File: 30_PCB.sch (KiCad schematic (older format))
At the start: 35 parts, among them J1 IPM-165-Radar, J10 TEST_VCC, J11 TEST_OUT, J2 TEST_AMPLIN, J3 TEST_AMPL1_OUT, J4 TEST_AMPL2_OUT, J6 TEST_GNDD, J7 TEST_GNDD, J8 TEST_GNDA, J9 TEST_GNDA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

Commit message: PCB R0.5/Schema R0.6
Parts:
- added R12: 1k, Resistor_SMD:R_1206_3216Metric_Pad1.42x1.75mm_HandSolder, symbol Device:R
- added unit 3 of U1
- C1, C2, C5: footprint Capacitor_THT:C_Radial_D5.0mm_H11.0mm_P2.00mm -> Capacitor_THT:CP_Radial_D5.0mm_P2.00mm
- C4: footprint Capacitor_THT:C_Rect_L7.2mm_W3.5mm_P5.00mm_FKS2_FKP2_MKS2_MKP2 -> Capacitor_THT:C_Rect_L7.2mm_W2.5mm_P5.00mm_FKS2_FKP2_MKS2_MKP2
- C6: footprint Capacitor_THT:C_Rect_L7.2mm_W5.5mm_P5.00mm_FKS2_FKP2_MKS2_MKP2 -> Capacitor_THT:C_Rect_L7.2mm_W4.5mm_P5.00mm_FKS2_FKP2_MKS2_MKP2
- D1, D2, D3, D4: footprint Diode_SMD:D_1206_3216Metric -> Diode_SMD:D_1206_3216Metric_Pad1.42x1.75mm_HandSolder
- R10, R11, R7, R9: footprint Resistor_SMD:R_1206_3216Metric -> Resistor_SMD:R_1206_3216Metric_Pad1.42x1.75mm_HandSolder
- XA1: symbol Arduino_SDHD:Arduino_Uno_Shield -> 30_PCB-rescue:Arduino_Uno_Shield-Arduino_SDHD
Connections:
- net GNDA: now also U1.4 (V-)
- net GNDD: now also R12.1
- net VCC: now also U1.8 (V+)
- net at SW1.2, SW1.4, XA1.D4: now also R12.2
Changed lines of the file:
@@
 Title "24GHz Radar Movement Detector"
 Date "2020-05-5"
-Rev "R0.5"
+Rev "R0.6"
 Comp "Hochschule Darmstadt"
 Comment1 ""
@@
 F 0 "C5" V 3625 4300 50  0000 C CNN
 F 1 "4.7u" V 3716 4300 50  0000 C CNN
-F 2 "Capacitor_THT:C_Radial_D5.0mm_H11.0mm_P2.00mm" H 3850 4300 50  0001 C CNN
+F 2 "Capacitor_THT:CP_Radial_D5.0mm_P2.00mm" H 3850 4300 50  0001 C CNN
 F 3 "~" H 3850 4300 50  0001 C CNN
 	1    3850 4300
@@
 F 0 "C2" V 1925 4400 50  0000 C CNN
 F 1 "4.7u" V 1834 4400 50  0000 C CNN
-F 2 "Capacitor_THT:C_Radial_D5.0mm_H11.0mm_P2.00mm" H 1700 4400 50  0001 C CNN
+F 2 "Capacitor_THT:CP_Radial_D5.0mm_P2.00mm" H 1700 4400 50  0001 C CNN
 F 3 "~" H 1700 4400 50  0001 C CNN
 	1    1700 4400
@@
 F 0 "C6" V 4698 5450 50  0000 C CNN
 F 1 "3.3n" V 4789 5450 50  0000 C CNN
-F 2 "Capacitor_THT:C_Rect_L7.2mm_W5.5mm_P5.00mm_FKS2_FKP2_MKS2_MKP2" H 4988 5300 50  0001 C CNN
+F 2 "Capacitor_THT:C_Rect_L7.2mm_W4.5mm_P5.00mm_FKS2_FKP2_MKS2_MKP2" H 4988 5300 50  0001 C CNN
 F 3 "~" H 4950 5450 50  0001 C CNN
 	1    4950 5450
@@
 F 0 "C1" H 1288 3146 50  0000 L CNN
 F 1 "22u" H 1288 3055 50  0000 L CNN
-F 2 "Capacitor_THT:C_Radial_D5.0mm_H11.0mm_P2.00mm" H 1200 3100 50  0001 C CNN
+F 2 "Capacitor_THT:CP_Radial_D5.0mm_P2.00mm" H 1200 3100 50  0001 C CNN
 F 3 "~" H 1200 3100 50  0001 C CNN
 	1    1200 3100
@@
 F 0 "C4" H 3238 3196 50  0000 L CNN
 F 1 "100n" H 3238 3105 50  0000 L CNN
-F 2 "Capacitor_THT:C_Rect_L7.2mm_W3.5mm_P5.00mm_FKS2_FKP2_MKS2_MKP2" H 3150 3150 50  0001 C CNN
+F 2 "Capacitor_THT:C_Rect_L7.2mm_W2.5mm_P5.00mm_FKS2_FKP2_MKS2_MKP2" H 3150 3150 50  0001 C CNN
 F 3 "~" H 3150 3150 50  0001 C CNN
 	1    3150 3150
@@
 $EndComp
 $Comp
-L Arduino_SDHD:Arduino_Uno_Shield XA1
+L 30_PCB-rescue:Arduino_Uno_Shield-Arduino_SDHD XA1
 U 1 1 5EBD5CC3
 P 7800 4050
@@
 F 0 "D2" H 9700 4150 50  0000 R CNN
 F 1 "GREEN" H 9500 4350 50  0000 R CNN
-F 2 "Diode_SMD:D_1206_3216Metric" H 9600 4250 50  0001 C CNN
+F 2 "Diode_SMD:D_1206_3216Metric_Pad1.42x1.75mm_HandSolder" H 9600 4250 50  0001 C CNN
 F 3 "~" H 9600 4250 50  0001 C CNN
 	1    9600 4250
@@
 F 0 "R11" H 10250 3900 50  0000 L CNN
 F 1 "220" V 10100 3650 50  0000 L CNN
-F 2 "Resistor_SMD:R_1206_3216Metric" V 10130 3750 50  0001 C CNN
+F 2 "Resistor_SMD:R_1206_3216Metric_Pad1.42x1.75mm_HandSolder" V 10130 3750 50  0001 C CNN
 F 3 "~" H 10200 3750 50  0001 C CNN
 	1    10200 3750
@@
 F 0 "R10" H 9950 3900 50  0000 L CNN
 F 1 "220" V 9800 3650 50  0000 L CNN
-F 2 "Resistor_SMD:R_1206_3216Metric" V 9830 3750 50  0001 C CNN
+F 2 "Resistor_SMD:R_1206_3216Metric_Pad1.42x1.75mm_HandSolder" V 9830 3750 50  0001 C CNN
 F 3 "~" H 9900 3750 50  0001 C CNN
 	1    9900 3750
@@
 F 0 "R9" H 9650 3900 50  0000 L CNN
 F 1 "220" V 9500 3650 50  0000 L CNN
-F 2 "Resistor_SMD:R_1206_3216Metric" V 9530 3750 50  0001 C CNN
+F 2 "Resistor_SMD:R_1206_3216Metric_Pad1.42x1.75mm_HandSolder" V 9530 3750 50  0001 C CNN
 F 3 "~" H 9600 3750 50  0001 C CNN
 	1    9600 3750
@@
 F 0 "D3" H 10000 4150 50  0000 R CNN
 F 1 "YELLOW" H 9850 4350 50  0000 R CNN
-F 2 "Diode_SMD:D_1206_3216Metric" H 9900 4250 50  0001 C CNN
+F 2 "Diode_SMD:D_1206_3216Metric_Pad1.42x1.75mm_HandSolder" H 9900 4250 50  0001 C CNN
 F 3 "~" H 9900 4250 50  0001 C CNN
 	1    9900 4250
@@
 F 0 "D4" H 10300 4150 50  0000 R CNN
 F 1 "RED" H 10050 4350 50  0000 R CNN
-F 2 "Diode_SMD:D_1206_3216Metric" H 10200 4250 50  0001 C CNN
+F 2 "Diode_SMD:D_1206_3216Metric_Pad1.42x1.75mm_HandSolder" H 10200 4250 50  0001 C CNN
 F 3 "~" H 10200 4250 50  0001 C CNN
 	1    10200 4250
@@
 F 0 "R7" H 5370 1196 50  0000 L CNN
 F 1 "220" H 5370 1105 50  0000 L CNN
-F 2 "Resistor_SMD:R_1206_3216Metric" V 5230 1150 50  0001 C CNN
+F 2 "Resistor_SMD:R_1206_3216Metric_Pad1.42x1.75mm_HandSolder" V 5230 1150 50  0001 C CNN
 F 3 "~" H 5300 1150 50  0001 C CNN
 	1    5300 1150
@@
 F 0 "D1" V 5339 1483 50  0000 R CNN
 F 1 "LED_POWER" V 5248 1483 50  0000 R CNN
-F 2 "Diode_SMD:D_1206_3216Metric" H 5300 1600 50  0001 C CNN
+F 2 "Diode_SMD:D_1206_3216Metric_Pad1.42x1.75mm_HandSolder" H 5300 1600 50  0001 C CNN
 F 3 "~" H 5300 1600 50  0001 C CNN
 	1    5300 1600
@@
 	6100 5550 6100 2300
 Wire Wire Line
-	9100 3200 10350 3200
+	9100 3200 9950 3200
 Wire Wire Line
 	9100 3300 10200 3300
@@
 Wire Notes Line
 	6100 5550 9250 5550
+$Comp
+L Device:R R12
+U 1 1 5EC0B5AD
+P 9950 2750
+F 0 "R12" H 10000 2900 50  0000 L CNN
+F 1 "1k" V 9850 2650 50  0000 L CNN
+F 2 "Resistor_SMD:R_1206_3216Metric_Pad1.42x1.75mm_HandSolder" V 9880 2750 50  0001 C CNN
+F 3 "~" H 9950 2750 50  0001 C CNN
+	1    9950 2750
+	1    0    0    -1
+$EndComp
+Wire Wire Line
+	9950 2900 9950 3200
+Connection ~ 9950 3200
+Wire Wire Line
+	9950 3200 10350 3200
+Wire Wire Line
+	9950 2600 9950 2400
+Wire Wire Line
+	9950 2400 9600 2400
+Wire Wire Line
+	9600 2400 9600 2650
+$Comp
+L power:GNDD #PWR02
+U 1 1 5EC13B78
+P 9600 2650
+F 0 "#PWR02" H 9600 2400 50  0001 C CNN
+F 1 "GNDD" H 9604 2495 50  0000 C CNN
+F 2 "" H 9600 2650 50  0001 C CNN
+F 3 "" H 9600 2650 50  0001 C CNN
+	1    9600 2650
+	1    0    0    -1
+$EndComp
+$Comp
+L Amplifier_Operational:LMV358 U1
+U 3 1 5EC51FA1
+P 5200 3000
+F 0 "U1" H 5158 3046 50  0000 L CNN
+F 1 "LMV358" H 5158 2955 50  0000 L CNN
+F 2 "Package_DIP:DIP-8_W7.62mm_Socket" H 5200 3000 50  0001 C CNN
+F 3 "http://www.ti.com/lit/ds/symlink/lmv324.pdf" H 5200 3000 50  0001 C CNN
+	3    5200 3000
+	1    0    0    -1
+$EndComp
+$Comp
+L power:VCC #PWR03
+U 1 1 5EC54F45
+P 5100 2700
+F 0 "#PWR03" H 5100 2550 50  0001 C CNN
+F 1 "VCC" H 5117 2873 50  0000 C CNN
+F 2 "" H 5100 2700 50  0001 C CNN
+F 3 "" H 5100 2700 50  0001 C CNN
+	1    5100 2700
+	1    0    0    -1
+$EndComp
+$Comp
+L power:GNDA #PWR04
+U 1 1 5EC579B8
+P 5100 3300
+F 0 "#PWR04" H 5100 3050 50  0001 C CNN
+F 1 "GNDA" V 5100 3100 50  0000 C CNN
+F 2 "" H 5100 3300 50  0001 C CNN
+F 3 "" H 5100 3300 50  0001 C CNN
+	1    5100 3300
+	1    0    0    -1
+$EndComp
+$Comp
+L h-DA_LOGO_EESCHEMA:LOGO #G?
+U 1 1 5EBF6885
+P 10250 7200
+F 0 "#G?" H 10250 6445 60  0001 C CNN
+F 1 "LOGO" H 10250 7955 60  0001 C CNN
+F 2 "" H 10250 7200 50  0001 C CNN
+F 3 "" H 10250 7200 50  0001 C CNN
+	1    10250 7200
+	1    0    0    -1
+$EndComp
 $EndSCHEMATC

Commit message: PCB R0.6/Schema R0.7--most likely final version
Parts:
- R1, R2, R3, R4, R5, R6, R8: footprint Resistor_THT:R_Axial_DIN0204_L3.6mm_D1.6mm_P7.62mm_Horizontal -> Resistor_THT:R_Axial_DIN0207_L6.3mm_D2.5mm_P7.62mm_Horizontal
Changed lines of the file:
@@
 Title "24GHz Radar Movement Detector"
 Date "2020-05-5"
-Rev "R0.6"
+Rev "R0.7"
 Comp "Hochschule Darmstadt"
 Comment1 ""
@@
 F 0 "R5" V 4093 4300 50  0000 C CNN
 F 1 "2.2k" V 4184 4300 50  0000 C CNN
-F 2 "Resistor_THT:R_Axial_DIN0204_L3.6mm_D1.6mm_P7.62mm_Horizontal" V 4230 4300 50  0001 C CNN
+F 2 "Resistor_THT:R_Axial_DIN0207_L6.3mm_D2.5mm_P7.62mm_Horizontal" V 4230 4300 50  0001 C CNN
 F 3 "~" H 4300 4300 50  0001 C CNN
 	1    4300 4300
@@
 F 0 "R3" V 1993 4400 50  0000 C CNN
 F 1 "2.2k" V 2084 4400 50  0000 C CNN
-F 2 "Resistor_THT:R_Axial_DIN0204_L3.6mm_D1.6mm_P7.62mm_Horizontal" V 2130 4400 50  0001 C CNN
+F 2 "Resistor_THT:R_Axial_DIN0207_L6.3mm_D2.5mm_P7.62mm_Horizontal" V 2130 4400 50  0001 C CNN
 F 3 "~" H 2200 4400 50  0001 C CNN
 	1    2200 4400
@@
 F 0 "R1" H 2070 2496 50  0000 L CNN
 F 1 "1k" H 2070 2405 50  0000 L CNN
-F 2 "Resistor_THT:R_Axial_DIN0204_L3.6mm_D1.6mm_P7.62mm_Horizontal" V 1930 2450 50  0001 C CNN
+F 2 "Resistor_THT:R_Axial_DIN0207_L6.3mm_D2.5mm_P7.62mm_Horizontal" V 1930 2450 50  0001 C CNN
 F 3 "~" H 2000 2450 50  0001 C CNN
 	1    2000 2450
@@
 F 0 "R2" H 2070 3146 50  0000 L CNN
 F 1 "1k" H 2070 3055 50  0000 L CNN
-F 2 "Resistor_THT:R_Axial_DIN0204_L3.6mm_D1.6mm_P7.62mm_Horizontal" V 1930 3100 50  0001 C CNN
+F 2 "Resistor_THT:R_Axial_DIN0207_L6.3mm_D2.5mm_P7.62mm_Horizontal" V 1930 3100 50  0001 C CNN
 F 3 "~" H 2000 3100 50  0001 C CNN
 	1    2000 3100
@@
 F 0 "R6" V 4743 5050 50  0000 C CNN
 F 1 "100k" V 4834 5050 50  0000 C CNN
-F 2 "Resistor_THT:R_Axial_DIN0204_L3.6mm_D1.6mm_P7.62mm_Horizontal" V 4880 5050 50  0001 C CNN
+F 2 "Resistor_THT:R_Axial_DIN0207_L6.3mm_D2.5mm_P7.62mm_Horizontal" V 4880 5050 50  0001 C CNN
 F 3 "~" H 4950 5050 50  0001 C CNN
 	1    4950 5050
@@
 F 0 "R8" V 5493 4200 50  0000 C CNN
 F 1 "100" V 5584 4200 50  0000 C CNN
-F 2 "Resistor_THT:R_Axial_DIN0204_L3.6mm_D1.6mm_P7.62mm_Horizontal" V 5630 4200 50  0001 C CNN
+F 2 "Resistor_THT:R_Axial_DIN0207_L6.3mm_D2.5mm_P7.62mm_Horizontal" V 5630 4200 50  0001 C CNN
 F 3 "~" H 5700 4200 50  0001 C CNN
 	1    5700 4200
@@
 F 0 "R4" V 2793 5050 50  0000 C CNN
 F 1 "220k" V 2884 5050 50  0000 C CNN
-F 2 "Resistor_THT:R_Axial_DIN0204_L3.6mm_D1.6mm_P7.62mm_Horizontal" V 2930 5050 50  0001 C CNN
+F 2 "Resistor_THT:R_Axial_DIN0207_L6.3mm_D2.5mm_P7.62mm_Horizontal" V 2930 5050 50  0001 C CNN
 F 3 "~" H 3000 5050 50  0001 C CNN
 	1    3000 5050
@@
 $EndComp
 $Comp
-L h-DA_LOGO_EESCHEMA:LOGO #G?
+L h-DA_LOGO_EESCHEMA:LOGO #G1
 U 1 1 5EBF6885
 P 10250 7200
-F 0 "#G?" H 10250 6445 60  0001 C CNN
+F 0 "#G1" H 10250 6445 60  0001 C CNN
 F 1 "LOGO" H 10250 7955 60  0001 C CNN
 F 2 "" H 10250 7200 50  0001 C CNN

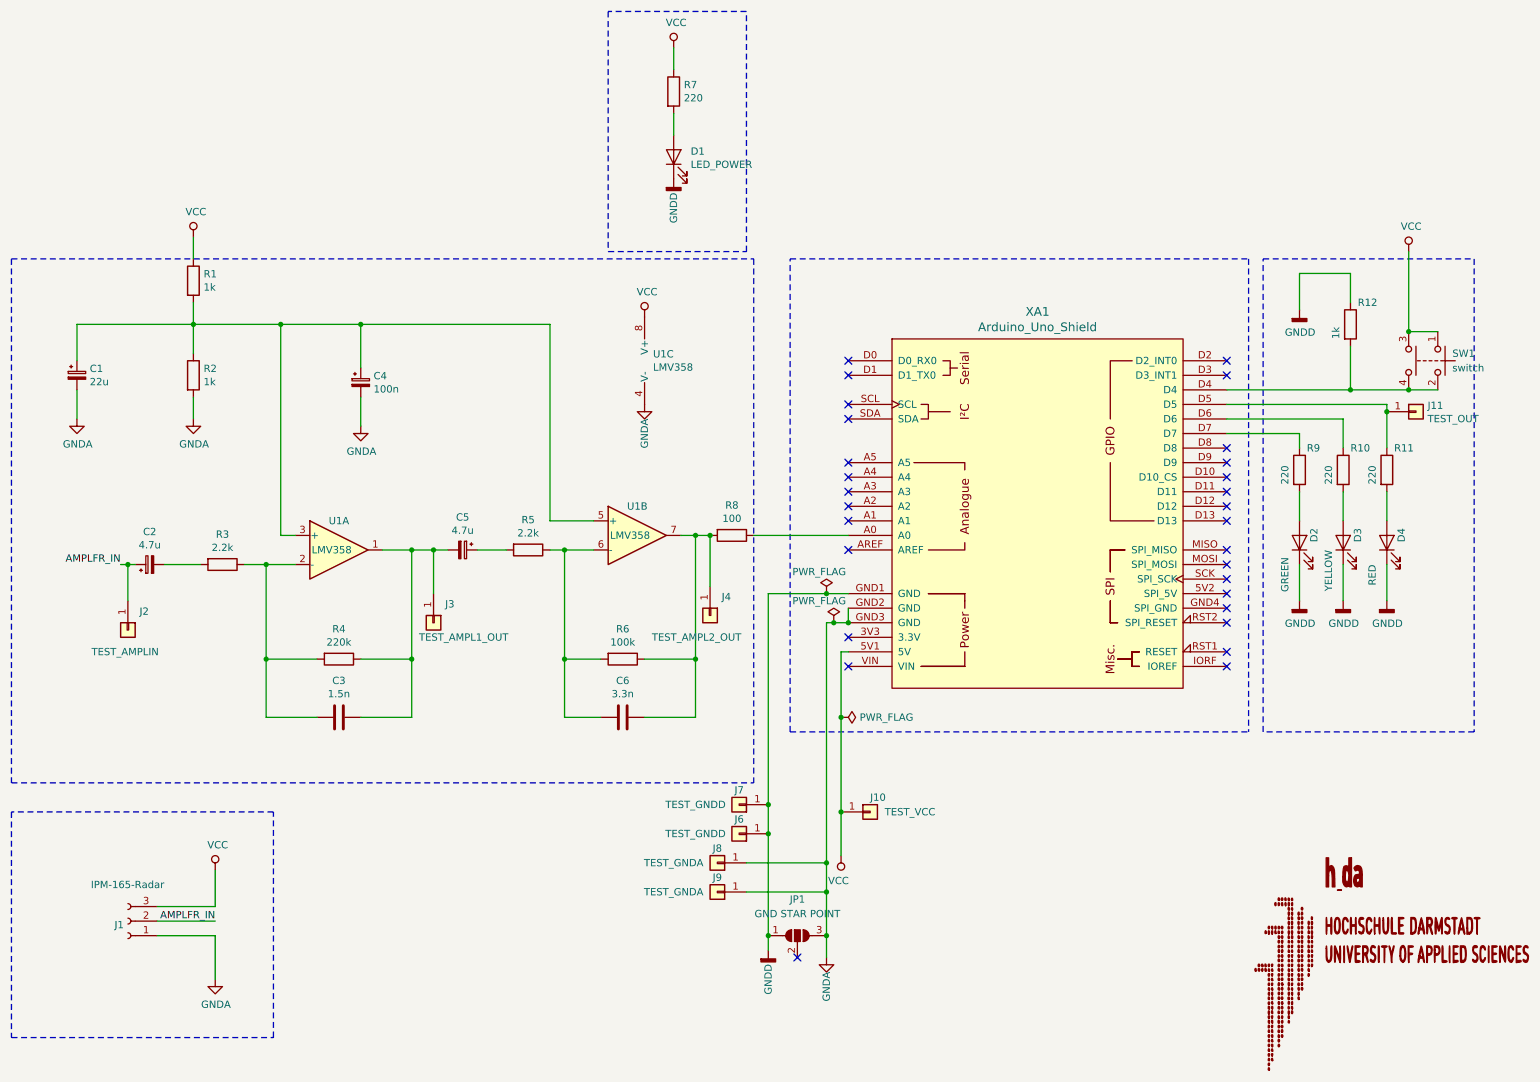
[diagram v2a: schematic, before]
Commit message: PCB R0.7/Schema R0.8 -- Descriptions added,minor modification,Final Version
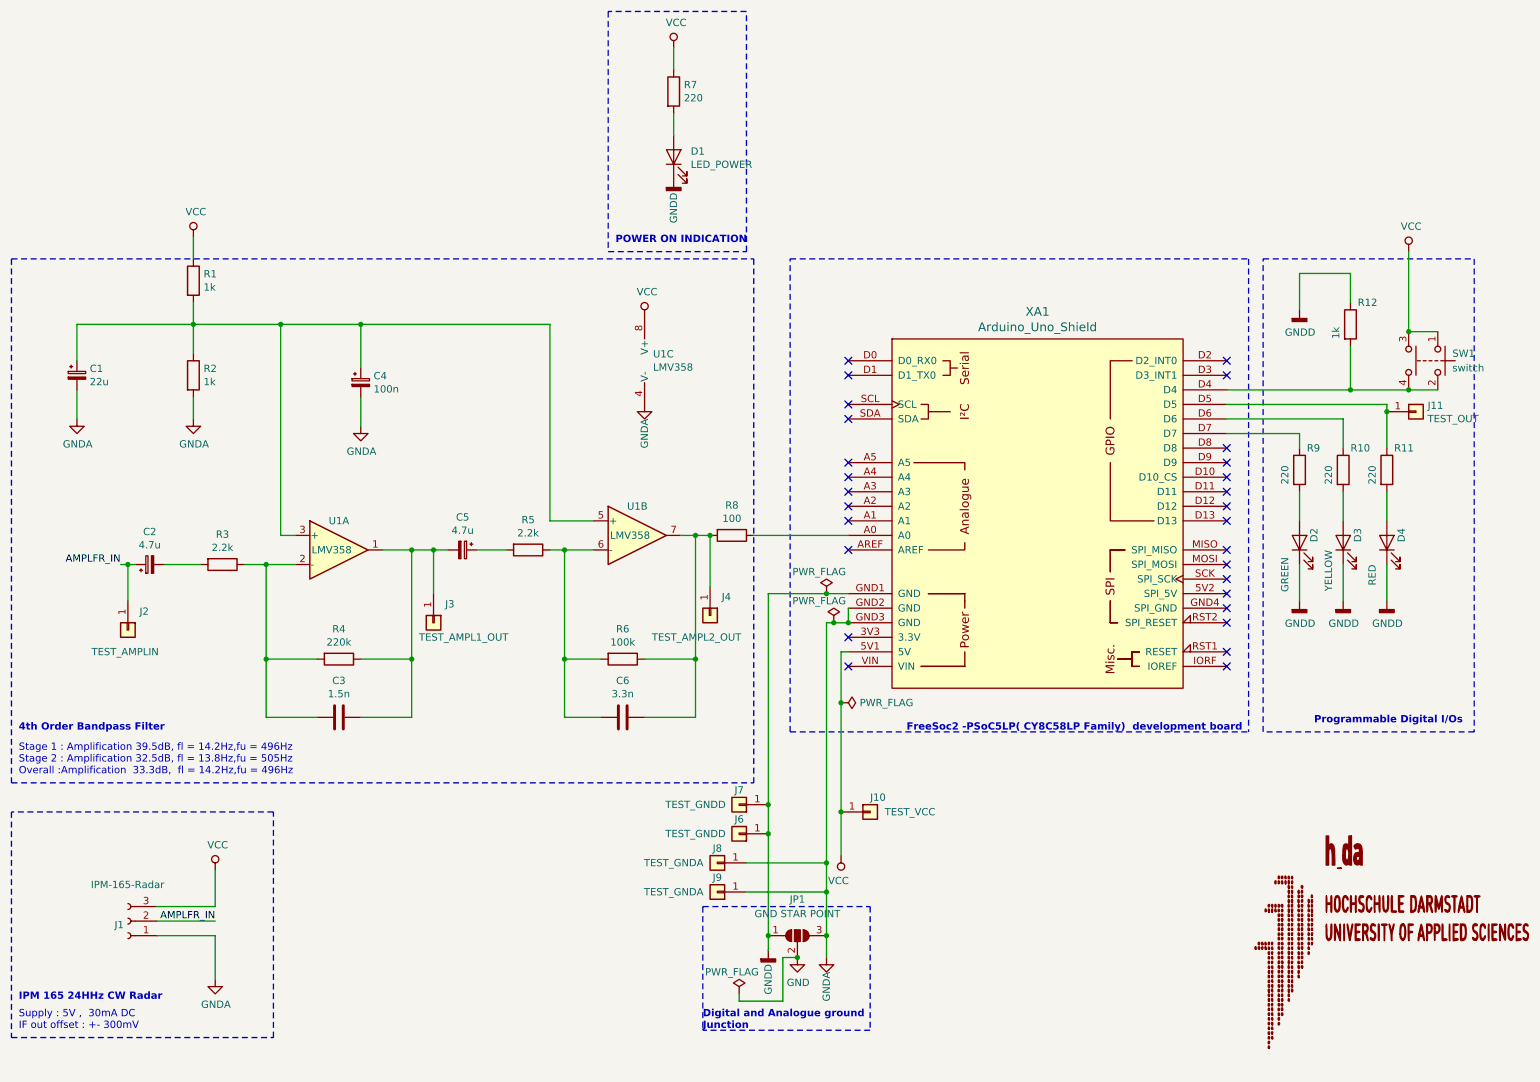
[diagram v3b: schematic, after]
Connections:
- net GND: now reaches JP1.2 (C)
- no-connect marks 29 -> 28
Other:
- note added: "4th Order Bandpass Filter"
- note added: "Digital and Analogue ground\nJunction"
- note added: "FreeSoc2 -PSoC5LP( CY8C58LP Family) development board"
- note added: "IPM 165 24HHz CW Radar"
- note added: "POWER ON INDICATION"
- note added: "Programmable Digital I/Os"
- note added: "Stage 1 : Amplification 39.5dB, fl = 14.2Hz,fu = 496Hz\nStage 2 : Amplification 32.5dB, fl = 13.8Hz,fu = 505Hz\nOverall :Amplification 33.3dB, fl = 14.2Hz,fu = 496Hz"
- note added: "Supply : 5V , 30mA DC\nIF out offset : +- 300mV"
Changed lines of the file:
@@
 Title "24GHz Radar Movement Detector"
 Date "2020-05-5"
-Rev "R0.7"
+Rev "R0.8"
 Comp "Hochschule Darmstadt"
 Comment1 ""
@@
 L power:PWR_FLAG #FLG0101
 U 1 1 5ECC74C0
-P 6450 5450
-F 0 "#FLG0101" H 6450 5525 50  0001 C CNN
-F 1 "PWR_FLAG" V 6450 5578 50  0000 L CNN
-F 2 "" H 6450 5450 50  0001 C CNN
-F 3 "~" H 6450 5450 50  0001 C CNN
-	1    6450 5450
+P 6450 5350
+F 0 "#FLG0101" H 6450 5425 50  0001 C CNN
+F 1 "PWR_FLAG" V 6450 5478 50  0000 L CNN
+F 2 "" H 6450 5350 50  0001 C CNN
+F 3 "~" H 6450 5350 50  0001 C CNN
+	1    6450 5350
 	0    1    1    0
 $EndComp
@@
 	5950 4600 6350 4600
 Wire Wire Line
-	6450 5000 6450 5450
+	6450 5000 6450 5350
 Wire Wire Line
 	6450 5000 6500 5000
-Connection ~ 6450 5450
-Wire Wire Line
-	6450 5450 6450 6100
+Connection ~ 6450 5350
 Connection ~ 6350 4600
 Wire Wire Line
@@
 Wire Wire Line
 	6350 6650 6350 6950
-NoConn ~ 6150 7100
 Wire Wire Line
 	6500 4700 6500 4800
@@
 L h-DA_LOGO_EESCHEMA:LOGO #G1
 U 1 1 5EBF6885
-P 10250 7200
-F 0 "#G1" H 10250 6445 60  0001 C CNN
-F 1 "LOGO" H 10250 7955 60  0001 C CNN
-F 2 "" H 10250 7200 50  0001 C CNN
-F 3 "" H 10250 7200 50  0001 C CNN
-	1    10250 7200
-	1    0    0    -1
-$EndComp
+P 10250 7050
+F 0 "#G1" H 10250 6295 60  0001 C CNN
+F 1 "LOGO" H 10250 7805 60  0001 C CNN
+F 2 "" H 10250 7050 50  0001 C CNN
+F 3 "" H 10250 7050 50  0001 C CNN
+	1    10250 7050
+	1    0    0    -1
+$EndComp
+Text Notes 800  5550 0    50   ~ 10
+4th Order Bandpass Filter
+Text Notes 800  5850 0    50   ~ 0
+Stage 1 : Amplification 39.5dB, fl = 14.2Hz,fu = 496Hz\nStage 2 : Amplification 32.5dB, fl = 13.8Hz,fu = 505Hz\nOverall :Amplification  33.3dB,  fl = 14.2Hz,fu = 496Hz
+Text Notes 800  7400 0    50   ~ 10
+IPM 165 24HHz CW Radar
+Text Notes 800  7600 0    50   ~ 0
+Supply : 5V ,  30mA DC\nIF out offset : +- 300mV
+Text Notes 4900 2200 0    50   ~ 10
+POWER ON INDICATION
+Text Notes 6900 5550 0    50   ~ 10
+FreeSoc2 -PSoC5LP( CY8C58LP Family)  development board
+Text Notes 9700 5500 0    50   ~ 10
+Programmable Digital I/Os
+Wire Notes Line
+	5500 6750 6650 6750
+Wire Notes Line
+	6650 7600 5500 7600
+Text Notes 5500 7600 0    50   ~ 10
+Digital and Analogue ground\nJunction
+Wire Notes Line
+	5500 6750 5500 7600
+Wire Notes Line
+	6650 6750 6650 7600
+Wire Wire Line
+	6450 5350 6450 6100
+$Comp
+L power:GND #PWR05
+U 1 1 5EC1B227
+P 6150 7100
+F 0 "#PWR05" H 6150 6850 50  0001 C CNN
+F 1 "GND" H 6155 6927 50  0000 C CNN
+F 2 "" H 6150 7100 50  0001 C CNN
+F 3 "" H 6150 7100 50  0001 C CNN
+	1    6150 7100
+	1    0    0    -1
+$EndComp
+$Comp
+L power:PWR_FLAG #FLG01
+U 1 1 5EC2314F
+P 5750 7350
+F 0 "#FLG01" H 5750 7425 50  0001 C CNN
+F 1 "PWR_FLAG" H 5700 7500 50  0000 C CNN
+F 2 "" H 5750 7350 50  0001 C CNN
+F 3 "~" H 5750 7350 50  0001 C CNN
+	1    5750 7350
+	1    0    0    -1
+$EndComp
+Wire Wire Line
+	5750 7350 5750 7400
+Wire Wire Line
+	5750 7400 6050 7400
+Wire Wire Line
+	6050 7400 6050 7100
+Wire Wire Line
+	6050 7100 6150 7100
+Connection ~ 6150 7100
 $EndSCHEMATC
